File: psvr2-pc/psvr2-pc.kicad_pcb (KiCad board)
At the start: 4 copper layers, 101.3 x 63.5 mm, 123 parts, among them IC1 SN65MLVD200D, IC2 SN65MLVD200D, J1 USB_C_Receptacle, J2 USB3_B_Micro, J3 DP_47272, J4 Barrel_Jack_Switch, J5 Conn_01x02_Pin, Q1 Si2301CDS, Q2 PN2222A, Q3 Si2301CDS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

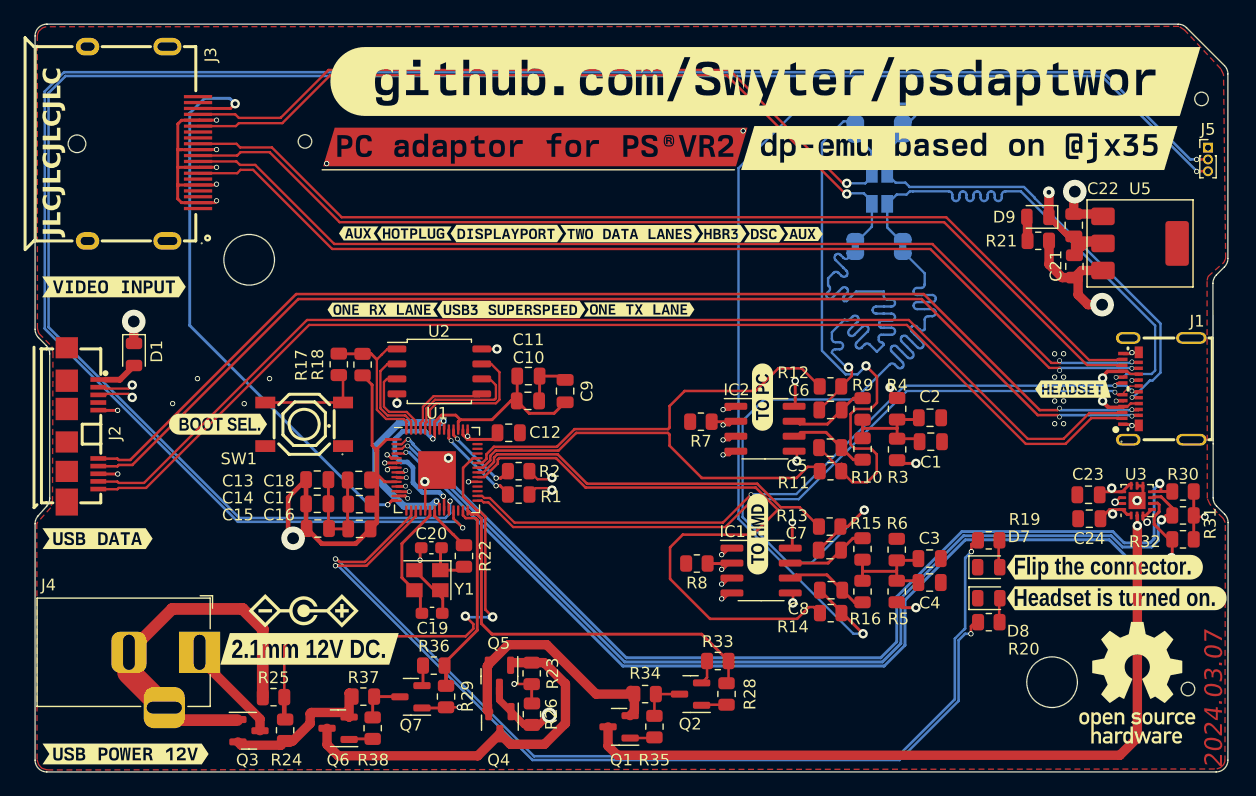
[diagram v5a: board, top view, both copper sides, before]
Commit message: Add more ground-stitching vias next to the AUX solder jumpers, as suggested by @mrandTX. Add more of them in the inner part of the USB Type-C receptacle, next to the part where some lanes go up.
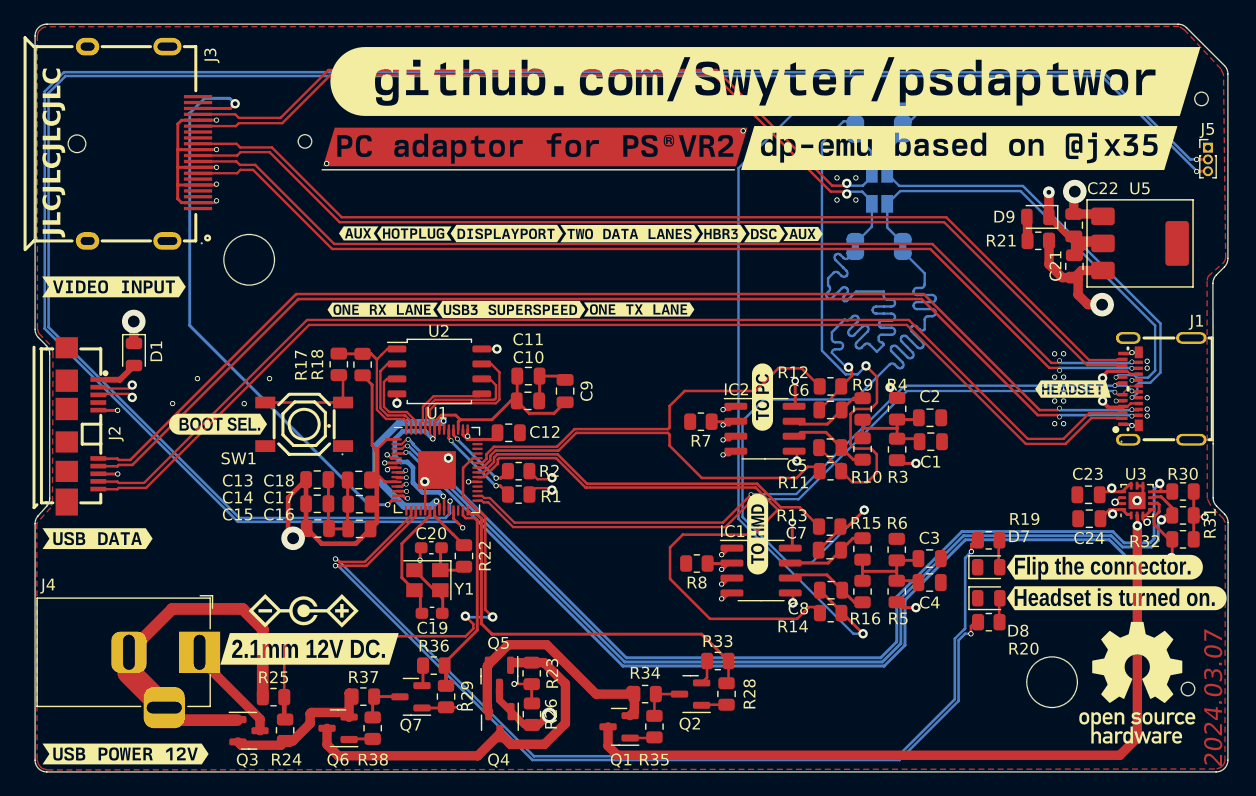
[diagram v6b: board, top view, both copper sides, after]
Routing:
- net /HMD_AUX_P: track 43.9 -> 39.8 mm
- net /HMD_LVDS_R: track 34.0 -> 31.4 mm
- net GND: vias 34 -> 43

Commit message: Move more or the HMD_LVDS_* lines next to the the microcontroller. Make the vias more far apart.
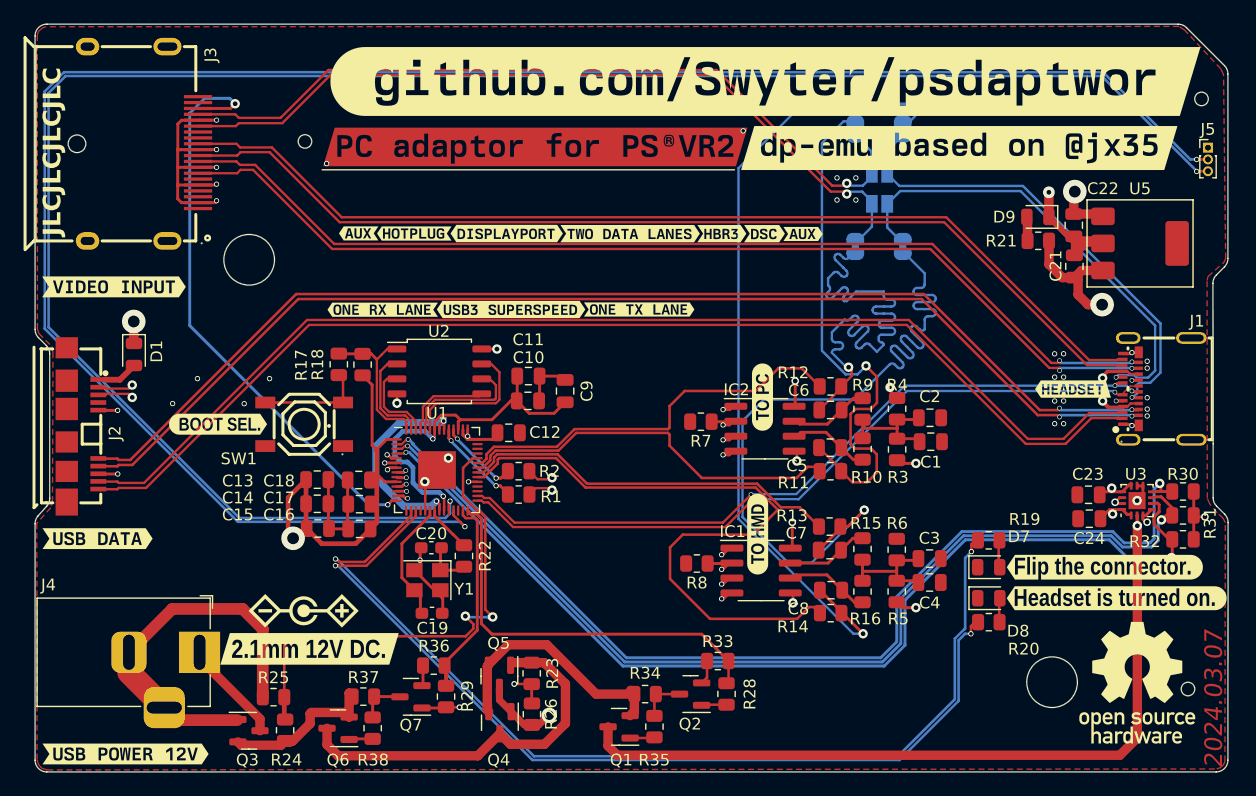
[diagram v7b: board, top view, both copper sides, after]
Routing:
- net /HMD_LVDS_R: track 31.4 -> 34.0 mm
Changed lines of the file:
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@@
   (via (at 44.227544 51.215) (size 0.4) (drill 0.3) (layers "F.Cu" "B.Cu") (net 17))
   (via (at 71 57.75) (size 0.45) (drill 0.3) (layers "F.Cu" "B.Cu") (net 17))
+  (segment (start 53.032248 60.164) (end 69.591026 60.164) (width 0.25) (layer "In2.Cu") (net 17))
   (segment (start 45.881622 53.0267) (end 45.894948 53.0267) (width 0.25) (layer "In2.Cu") (net 17))
-  (segment (start 50.618248 57.75) (end 71 57.75) (width 0.25) (layer "In2.Cu") (net 17))
-  (segment (start 44.695012 51.580085) (end 45.515 52.400074) (width 0.25) (layer "In2.Cu") (net 17))
-  (segment (start 45.515 52.400074) (end 45.515 52.660078) (width 0.25) (layer "In2.Cu") (net 17))
-  (segment (start 44.341814 51.215) (end 44.695012 51.568198) (width 0.25) (layer "In2.Cu") (net 17))
-  (segment (start 44.695012 51.568198) (end 44.695012 51.580085) (width 0.25) (layer "In2.Cu") (net 17))
-  (segment (start 44.227544 51.215) (end 44.341814 51.215) (width 0.25) (layer "In2.Cu") (net 17))
+  (segment (start 44.227544 51.215) (end 44.227544 51.219894) (width 0.25) (layer "In2.Cu") (net 17))
+  (segment (start 44.416764 51.28995) (end 44.695012 51.568198) (width 0.25) (layer "In2.Cu") (net 17))
+  (segment (start 45.515 52.476274) (end 45.515 52.660078) (width 0.25) (layer "In2.Cu") (net 17))
+  (segment (start 44.695012 51.568198) (end 44.695012 51.656286) (width 0.25) (layer "In2.Cu") (net 17))
+  (segment (start 44.2976 51.28995) (end 44.416764 51.28995) (width 0.25) (layer "In2.Cu") (net 17))
+  (segment (start 44.695012 51.656286) (end 45.515 52.476274) (width 0.25) (layer "In2.Cu") (net 17))
+  (segment (start 70.525 59.230026) (end 70.525 58.225) (width 0.25) (layer "In2.Cu") (net 17))
+  (segment (start 70.525 58.225) (end 71 57.75) (width 0.25) (layer "In2.Cu") (net 17))
   (segment (start 45.515 52.660078) (end 45.881622 53.0267) (width 0.25) (layer "In2.Cu") (net 17))
-  (segment (start 45.894948 53.0267) (end 50.618248 57.75) (width 0.25) (layer "In2.Cu") (net 17))
+  (segment (start 45.894948 53.0267) (end 53.032248 60.164) (width 0.25) (layer "In2.Cu") (net 17))
+  (segment (start 69.591026 60.164) (end 70.525 59.230026) (width 0.25) (layer "In2.Cu") (net 17))
+  (segment (start 44.227544 51.219894) (end 44.2976 51.28995) (width 0.25) (layer "In2.Cu") (net 17))
   (segment (start 71.639 58.403) (end 71.6385 58.4025) (width 0.25) (layer "F.Cu") (net 18))
   (segment (start 71.6385 58.4025) (end 71.5385 58.5025) (width 0.25) (layer "F.Cu") (net 18))
@@
   (via (at 44.220012 51.76495) (size 0.4) (drill 0.3) (layers "F.Cu" "B.Cu") (net 18))
   (via (at 71 59) (size 0.45) (drill 0.3) (layers "F.Cu" "B.Cu") (net 18))
-  (segment (start 44.384902 51.76495) (end 45.165 52.545048) (width 0.25) (layer "In2.Cu") (net 18))
+  (segment (start 71 59.25) (end 71 59) (width 0.25) (layer "In2.Cu") (net 18))
+  (segment (start 44.220012 51.76495) (end 44.308702 51.76495) (width 0.25) (layer "In2.Cu") (net 18))
+  (segment (start 45.165 52.805052) (end 45.736648 53.3767) (width 0.25) (layer "In2.Cu") (net 18))
+  (segment (start 45.749974 53.3767) (end 52.887274 60.514) (width 0.25) (layer "In2.Cu") (net 18))
+  (segment (start 45.165 52.621248) (end 45.165 52.805052) (width 0.25) (layer "In2.Cu") (net 18))
+  (segment (start 52.887274 60.514) (end 69.736 60.514) (width 0.25) (layer "In2.Cu") (net 18))
   (segment (start 45.736648 53.3767) (end 45.749974 53.3767) (width 0.25) (layer "In2.Cu") (net 18))
-  (segment (start 44.220012 51.76495) (end 44.384902 51.76495) (width 0.25) (layer "In2.Cu") (net 18))
-  (segment (start 45.165 52.545048) (end 45.165 52.805052) (width 0.25) (layer "In2.Cu") (net 18))
-  (segment (start 45.165 52.805052) (end 45.736648 53.3767) (width 0.25) (layer "In2.Cu") (net 18))
-  (segment (start 52.887274 60.514) (end 69.736 60.514) (width 0.25) (layer "In2.Cu") (net 18))
-  (segment (start 71 59.25) (end 71 59) (width 0.25) (layer "In2.Cu") (net 18))
   (segment (start 69.736 60.514) (end 71 59.25) (width 0.25) (layer "In2.Cu") (net 18))
-  (segment (start 45.749974 53.3767) (end 52.887274 60.514) (width 0.25) (layer "In2.Cu") (net 18))
+  (segment (start 44.308702 51.76495) (end 45.165 52.621248) (width 0.25) (layer "In2.Cu") (net 18))
   (segment (start 44.233201 52.362999) (end 43.3945 52.362999) (width 0.25) (layer "F.Cu") (net 19))
   (segment (start 71.124 60.25) (end 71.639 59.735) (width 0.25) (layer "F.Cu") (net 19))
@@
   (via (at 44.2468 52.3748) (size 0.4) (drill 0.3) (layers "F.Cu" "B.Cu") (net 19))
   (via (at 71 60.25) (size 0.45) (drill 0.3) (layers "F.Cu" "B.Cu") (net 19))
+  (segment (start 44.815 52.773248) (end 44.815 52.950026) (width 0.25) (layer "In2.Cu") (net 19))
+  (segment (start 44.2468 52.495) (end 44.536752 52.495) (width 0.25) (layer "In2.Cu") (net 19))
   (segment (start 45.591674 53.7267) (end 45.605 53.7267) (width 0.25) (layer "In2.Cu") (net 19))
+  (segment (start 44.815 52.950026) (end 45.591674 53.7267) (width 0.25) (layer "In2.Cu") (net 19))
+  (segment (start 69.880975 60.864) (end 70.494975 60.25) (width 0.25) (layer "In2.Cu") (net 19))
+  (segment (start 44.536752 52.495) (end 44.815 52.773248) (width 0.25) (layer "In2.Cu") (net 19))
+  (segment (start 44.2468 52.3748) (end 44.2468 52.495) (width 0.25) (layer "In2.Cu") (net 19))
+  (segment (start 45.605 53.7267) (end 52.7423 60.864) (width 0.25) (layer "In2.Cu") (net 19))
+  (segment (start 70.494975 60.25) (end 71 60.25) (width 0.25) (layer "In2.Cu") (net 19))
   (segment (start 52.7423 60.864) (end 69.880975 60.864) (width 0.25) (layer "In2.Cu") (net 19))
-  (segment (start 45.605 53.7267) (end 52.7423 60.864) (width 0.25) (layer "In2.Cu") (net 19))
-  (segment (start 44.2468 52.3748) (end 44.416552 52.3748) (width 0.25) (layer "In2.Cu") (net 19))
-  (segment (start 44.815 52.773248) (end 44.815 52.950026) (width 0.25) (layer "In2.Cu") (net 19))
-  (segment (start 69.880975 60.864) (end 70.494975 60.25) (width 0.25) (layer "In2.Cu") (net 19))
-  (segment (start 70.494975 60.25) (end 71 60.25) (width 0.25) (layer "In2.Cu") (net 19))
-  (segment (start 44.815 52.950026) (end 45.591674 53.7267) (width 0.25) (layer "In2.Cu") (net 19))
-  (segment (start 44.416552 52.3748) (end 44.815 52.773248) (width 0.25) (layer "In2.Cu") (net 19))
   (segment (start 44.170248 52.97) (end 43.963247 52.762999) (width 0.25) (layer "F.Cu") (net 20))
   (segment (start 43.963247 52.762999) (end 43.3945 52.762999) (width 0.25) (layer "F.Cu") (net 20))
@@
   (segment (start 111.34 25.21) (end 111.34 25.183256) (width 0.2205) (layer "B.Cu") (net 94))
   (segment (start 103.257244 17.1005) (end 15.292756 17.1005) (width 0.2205) (layer "B.Cu") (net 94))
-  (segment (start 49.01 55.47) (end 48.232 54.692) (width 0.2205) (layer "F.Cu") (net 95))
-  (segment (start 48.232 54.692) (end 48.232 54.000499) (width 0.2205) (layer "F.Cu") (net 95))
+  (segment (start 48.232 54.407435) (end 48.232 54.000499) (width 0.2205) (layer "F.Cu") (net 95))
+  (segment (start 49.1998 55.372) (end 49.196565 55.372) (width 0.2205) (layer "F.Cu") (net 95))
+  (segment (start 49.196565 55.372) (end 48.232 54.407435) (width 0.2205) (layer "F.Cu") (net 95))
   (segment (start 111.34 24.19) (end 112.3 24.19) (width 0.2205) (layer "F.Cu") (net 95))
-  (via (at 49.01 55.47) (size 0.45) (drill 0.3) (layers "F.Cu" "B.Cu") (net 95))
+  (via (at 49.1998 55.372) (size 0.45) (drill 0.3) (layers "F.Cu" "B.Cu") (net 95))
   (via (at 111.34 24.19) (size 0.45) (drill 0.3) (layers "F.Cu" "B.Cu") (net 95))
-  (segment (start 103.39 16.78) (end 15.16 16.78) (width 0.2205) (layer "B.Cu") (net 95))
-  (segment (start 111.34 24.19) (end 110.8 24.19) (width 0.2205) (layer "B.Cu") (net 95))
-  (segment (start 13.52 18.42) (end 13.52 38.56) (width 0.2205) (layer "B.Cu") (net 95))
-  (segment (start 29.92 54.96) (end 48.5 54.96) (width 0.2205) (layer "B.Cu") (net 95))
-  (segment (start 13.52 38.56) (end 29.92 54.96) (width 0.2205) (layer "B.Cu") (net 95))
-  (segment (start 110.8 24.19) (end 103.39 16.78) (width 0.2205) (layer "B.Cu") (net 95))
-  (segment (start 15.16 16.78) (end 13.52 18.42) (width 0.2205) (layer "B.Cu") (net 95))
-  (segment (start 48.5 54.96) (end 49.01 55.47) (width 0.2205) (layer "B.Cu") (net 95))
+  (segment (start 15.16 16.78) (end 103.39 16.78) (width 0.2205) (layer "B.Cu") (net 95))
+  (segment (start 13.52 38.56) (end 13.52 18.42) (width 0.2205) (layer "B.Cu") (net 95))
+  (segment (start 29.92 54.96) (end 13.52 38.56) (width 0.2205) (layer "B.Cu") (net 95))
+  (segment (start 49.1998 55.372) (end 48.7878 54.96) (width 0.2205) (layer "B.Cu") (net 95))
+  (segment (start 48.7878 54.96) (end 29.92 54.96) (width 0.2205) (layer "B.Cu") (net 95))
+  (segment (start 103.39 16.78) (end 110.8 24.19) (width 0.2205) (layer "B.Cu") (net 95))
+  (segment (start 110.8 24.19) (end 111.34 24.19) (width 0.2205) (layer "B.Cu") (net 95))
+  (segment (start 13.52 18.42) (end 15.16 16.78) (width 0.2205) (layer "B.Cu") (net 95))
   (segment (start 81.155 43.4625) (end 81.155 43.51) (width 0.2) (layer "F.Cu") (net 97))
   (segment (start 82.05 42.5675) (end 82.05 42.1) (width 0.2205) (layer "F.Cu") (net 97))

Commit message: More LED resistor value calculation shenanigans. Update the comment text.
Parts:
- R19, R20: value 56K -> 68
- R21: value 86K -> 47
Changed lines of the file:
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@@
         (effects (font (size 1 1) (thickness 0.15)))
     )
-    (fp_text value "56K" (at 0 1.65) (layer "F.Fab")
+    (fp_text value "68" (at 0 1.65) (layer "F.Fab")
         (effects (font (size 1 1) (thickness 0.15)))
     )
@@
       (net 62 "/PC_HPD") (pinfunction "GPIO11") (pintype "bidirectional"))
     (pad "15" smd roundrect (at -2.6 3.4375) (size 0.2 0.875) (layers "F.Cu" "F.Paste" "F.Mask") (roundrect_rratio 0.25)
-      (net 69 "unconnected-(U1-GPIO12-Pad15)") (pinfunction "GPIO12") (pintype "bidirectional"))
+      (net 69 "unconnected-(U1-GPIO12-Pad15)") (pinfunction "GPIO12") (pintype "bidirectional+no_connect"))
     (pad "16" smd roundrect (at -2.2 3.4375) (size 0.2 0.875) (layers "F.Cu" "F.Paste" "F.Mask") (roundrect_rratio 0.25)
       (net 15 "/LED_CONN_WRONG_ORIENT") (pinfunction "GPIO13") (pintype "bidirectional"))
@@
       (net 16 "/LED_HMD_IS_READY") (pinfunction "GPIO14") (pintype "bidirectional"))
     (pad "18" smd roundrect (at -1.4 3.4375) (size 0.2 0.875) (layers "F.Cu" "F.Paste" "F.Mask") (roundrect_rratio 0.25)
-      (net 5 "unconnected-(U1-GPIO15-Pad18)") (pinfunction "GPIO15") (pintype "bidirectional"))
+      (net 5 "unconnected-(U1-GPIO15-Pad18)") (pinfunction "GPIO15") (pintype "bidirectional+no_connect"))
     (pad "19" smd roundrect (at -1 3.4375) (size 0.2 0.875) (layers "F.Cu" "F.Paste" "F.Mask") (roundrect_rratio 0.25)
       (net 23 "GND") (pinfunction "TESTEN") (pintype "input"))
@@
       (net 95 "/SWD") (pinfunction "SWD") (pintype "bidirectional"))
     (pad "26" smd roundrect (at 1.8 3.4375) (size 0.2 0.875) (layers "F.Cu" "F.Paste" "F.Mask") (roundrect_rratio 0.25)
-      (net 9 "unconnected-(U1-RUN-Pad26)") (pinfunction "RUN") (pintype "input"))
+      (net 9 "unconnected-(U1-RUN-Pad26)") (pinfunction "RUN") (pintype "input+no_connect"))
     (pad "27" smd roundrect (at 2.2 3.4375) (size 0.2 0.875) (layers "F.Cu" "F.Paste" "F.Mask") (roundrect_rratio 0.25)
       (net 64 "/HMD_ENABLE_VBUS_12V") (pinfunction "GPIO16") (pintype "bidirectional"))
@@
       (net 11 "/HMD_USB2_N") (pinfunction "GPIO19") (pintype "bidirectional"))
     (pad "31" smd roundrect (at 3.4375 1.8) (size 0.875 0.2) (layers "F.Cu" "F.Paste" "F.Mask") (roundrect_rratio 0.25)
-      (net 96 "unconnected-(U1-GPIO20-Pad31)") (pinfunction "GPIO20") (pintype "bidirectional"))
+      (net 96 "unconnected-(U1-GPIO20-Pad31)") (pinfunction "GPIO20") (pintype "bidirectional+no_connect"))
     (pad "32" smd roundrect (at 3.4375 1.4) (size 0.875 0.2) (layers "F.Cu" "F.Paste" "F.Mask") (roundrect_rratio 0.25)
-      (net 12 "unconnected-(U1-GPIO21-Pad32)") (pinfunction "GPIO21") (pintype "bidirectional"))
+      (net 12 "unconnected-(U1-GPIO21-Pad32)") (pinfunction "GPIO21") (pintype "bidirectional+no_connect"))
     (pad "33" smd roundrect (at 3.4375 1) (size 0.875 0.2) (layers "F.Cu" "F.Paste" "F.Mask") (roundrect_rratio 0.25)
       (net 36 "+3.3V") (pinfunction "IOVDD") (pintype "passive"))
@@
       (net 80 "/DC_JACK_VOLT_SENSE") (pinfunction "GPIO26_ADC0") (pintype "bidirectional"))
     (pad "39" smd roundrect (at 3.4375 -1.4) (size 0.875 0.2) (layers "F.Cu" "F.Paste" "F.Mask") (roundrect_rratio 0.25)
-      (net 14 "unconnected-(U1-GPIO27_ADC1-Pad39)") (pinfunction "GPIO27_ADC1") (pintype "bidirectional"))
+      (net 14 "unconnected-(U1-GPIO27_ADC1-Pad39)") (pinfunction "GPIO27_ADC1") (pintype "bidirectional+no_connect"))
     (pad "40" smd roundrect (at 3.4375 -1.8) (size 0.875 0.2) (layers "F.Cu" "F.Paste" "F.Mask") (roundrect_rratio 0.25)
-      (net 77 "unconnected-(U1-GPIO28_ADC2-Pad40)") (pinfunction "GPIO28_ADC2") (pintype "bidirectional"))
+      (net 77 "unconnected-(U1-GPIO28_ADC2-Pad40)") (pinfunction "GPIO28_ADC2") (pintype "bidirectional+no_connect"))
     (pad "41" smd roundrect (at 3.4375 -2.2) (size 0.875 0.2) (layers "F.Cu" "F.Paste" "F.Mask") (roundrect_rratio 0.25)
-      (net 78 "unconnected-(U1-GPIO29_ADC3-Pad41)") (pinfunction "GPIO29_ADC3") (pintype "bidirectional"))
+      (net 78 "unconnected-(U1-GPIO29_ADC3-Pad41)") (pinfunction "GPIO29_ADC3") (pintype "bidirectional+no_connect"))
     (pad "42" smd roundrect (at 3.4375 -2.6) (size 0.875 0.2) (layers "F.Cu" "F.Paste" "F.Mask") (roundrect_rratio 0.25)
       (net 36 "+3.3V") (pinfunction "IOVDD") (pintype "passive"))
@@
         (effects (font (size 1 1) (thickness 0.15)))
     )
-    (fp_text value "56K" (at 0 1.65) (layer "F.Fab")
+    (fp_text value "68" (at 0 1.65) (layer "F.Fab")
         (effects (font (size 1 1) (thickness 0.15)))
     )
@@
     (property "Sheetfile" "psvr2-pc.kicad_sch")
     (property "Sheetname" "")
+    (property "Sim.Device" "SUBCKT")
+    (property "Sim.Name" "Si2301CDS")
     (property "ki_description" "SOT-23 P-MOSFET enchancement mode transistor, 20V, 3.1A, 1.6W, Alternate KiCAD Library")
     (property "ki_keywords" "enchancement mosfet pmosfet p-mosfet pmos p-mos emos emosfet Si2301CDS")
@@
     (descr "LED SMD 0805 (2012 Metric), square (rectangular) end terminal, IPC_7351 nominal, (Body size source: https://docs.google.com/spreadsheets/d/1BsfQQcO9C6DZCsRaXUlFlo91Tg2WpOkGARC1WS5S8t0/edit?usp=sharing), generated with kicad-footprint-generator")
     (tags "LED")
+    (property "LCSC Part #" "C84256")
+    (property "Mfr. Part #" "NCD0805R1")
     (property "Sheetfile" "psvr2-pc.kicad_sch")
     (property "Sheetname" "")
@@
     (descr "LED SMD 0805 (2012 Metric), square (rectangular) end terminal, IPC_7351 nominal, (Body size source: https://docs.google.com/spreadsheets/d/1BsfQQcO9C6DZCsRaXUlFlo91Tg2WpOkGARC1WS5S8t0/edit?usp=sharing), generated with kicad-footprint-generator")
     (tags "LED")
+    (property "LCSC Part #" "C2296")
+    (property "Mfr. Part #" "KT-0805Y")
     (property "Sheetfile" "psvr2-pc.kicad_sch")
     (property "Sheetname" "")
@@
         (effects (font (size 1 1) (thickness 0.15)))
     )
-    (fp_text value "86K" (at 0 1.65) (layer "F.Fab")
+    (fp_text value "47" (at 0 1.65) (layer "F.Fab")
         (effects (font (size 1 1) (thickness 0.15)))
     )
@@
     (descr "LED SMD 0805 (2012 Metric), square (rectangular) end terminal, IPC_7351 nominal, (Body size source: https://docs.google.com/spreadsheets/d/1BsfQQcO9C6DZCsRaXUlFlo91Tg2WpOkGARC1WS5S8t0/edit?usp=sharing), generated with kicad-footprint-generator")
     (tags "LED")
+    (property "LCSC Part #" "C2297")
+    (property "Mfr. Part #" "KT-0805G")
     (property "Sheetfile" "psvr2-pc.kicad_sch")
     (property "Sheetname" "")
@@
     (descr "module CMS SOT223 4 pins, Alternate KiCad Library")
     (tags "CMS SOT")
-    (property "LSC Part #" "C6186")
+    (property "LCSC Part #" "C6186")
     (property "Mfr. Part #" "AMS1117-3.3")
     (property "Sheetfile" "psvr2-pc.kicad_sch")
